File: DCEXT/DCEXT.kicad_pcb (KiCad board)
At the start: 2 copper layers, 77 x 100.5 mm, 5 parts, among them U1 MPCIE-Socket

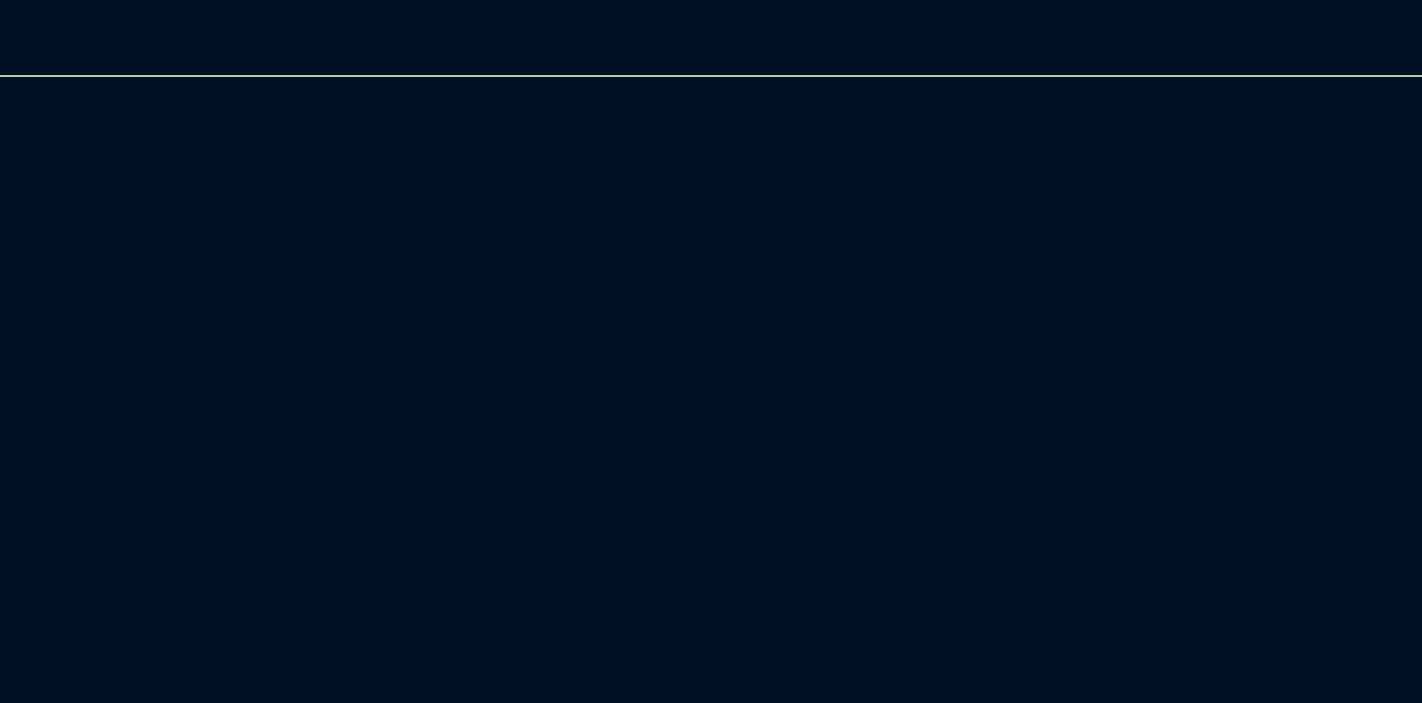
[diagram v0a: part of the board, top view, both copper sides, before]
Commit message: Add usb host connector and add more documentation
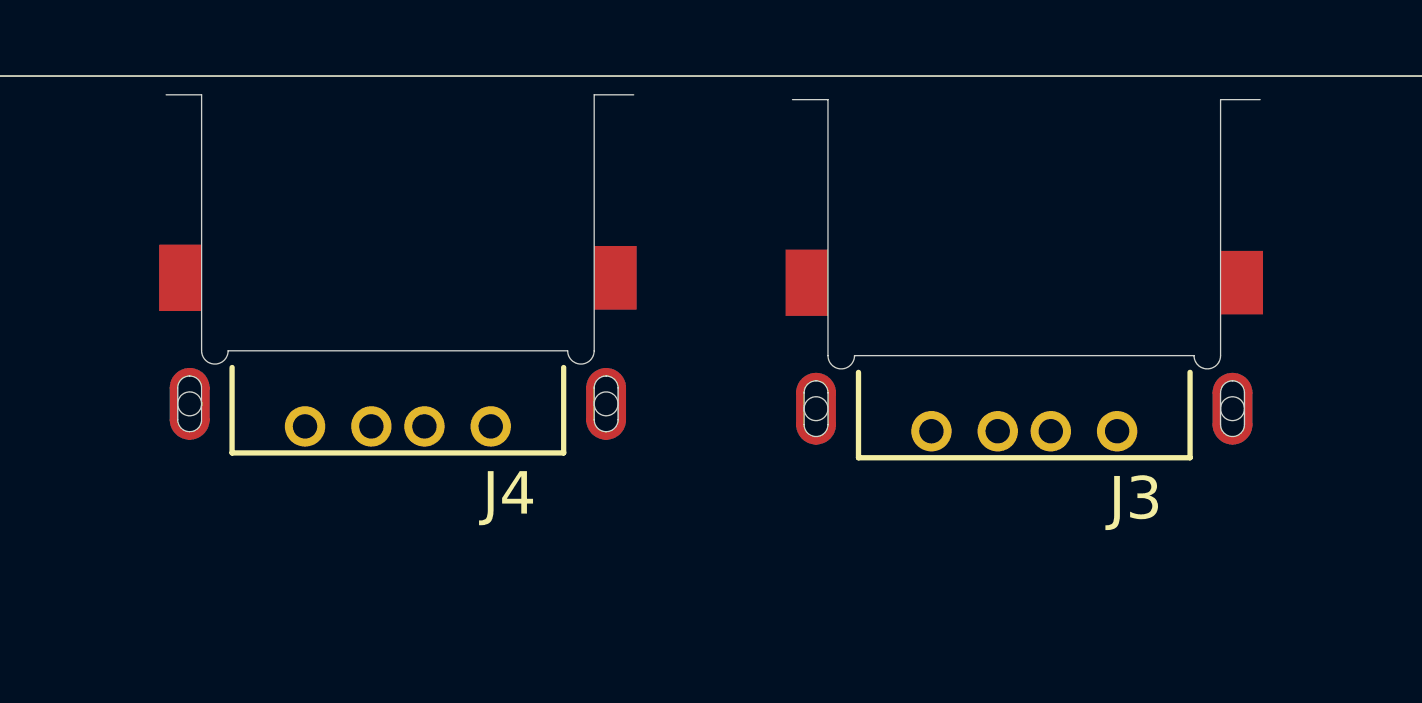
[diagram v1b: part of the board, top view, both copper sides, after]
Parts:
- added J3: USB1015-XX-X-X_REVC, DCEXT:GCT_USB1015-XX-X-X_REVC, F.Cu at (110.0, 49.5)
- added J4: USB1015-XX-X-X_REVC, DCEXT:GCT_USB1015-XX-X-X_REVC, F.Cu at (86.4, 49.3)
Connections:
- H1 pad 1: Net-(H1-Pad1) -> GND
- H2 pad 1: Net-(H2-Pad1) -> GND
- H3 pad 1: Net-(H3-Pad1) -> GND
- H4 pad 1: Net-(H4-Pad1) -> GND

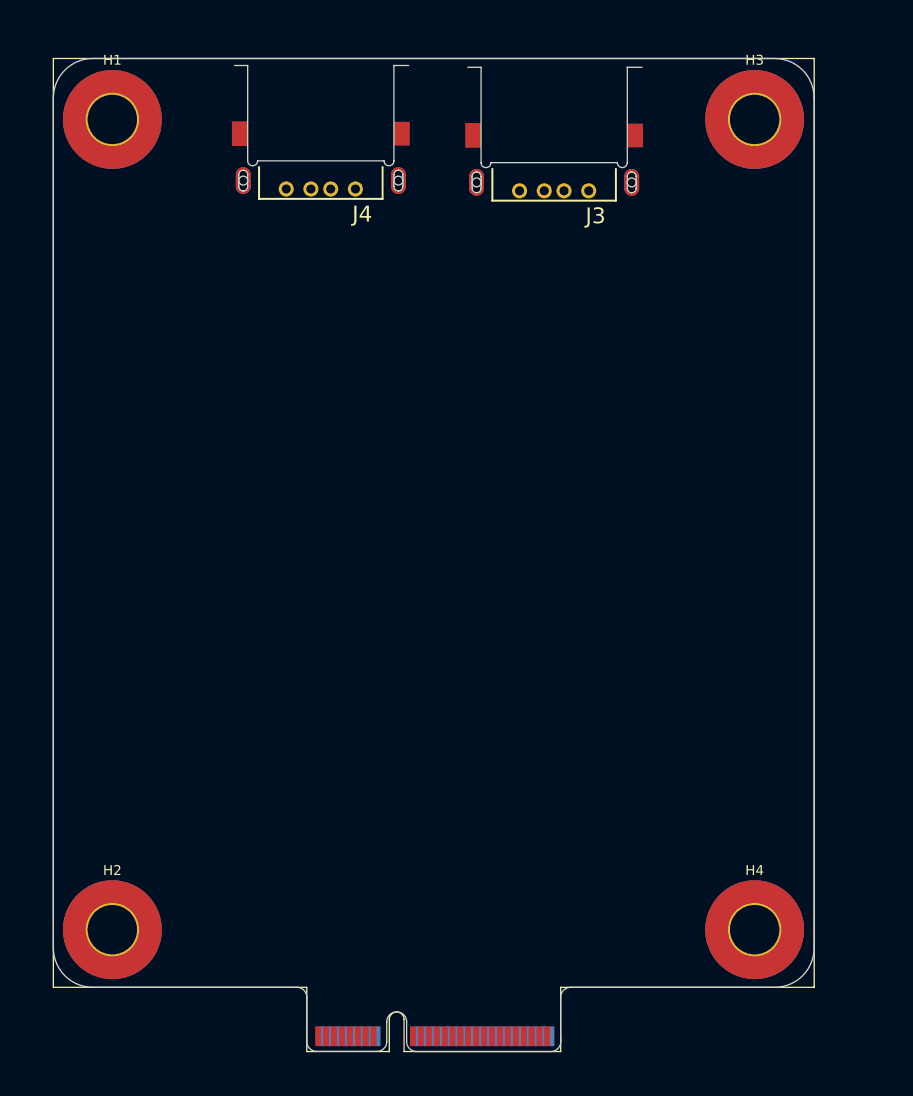
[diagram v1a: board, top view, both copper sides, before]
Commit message: Add usb protection, fan control and fpc connector for module
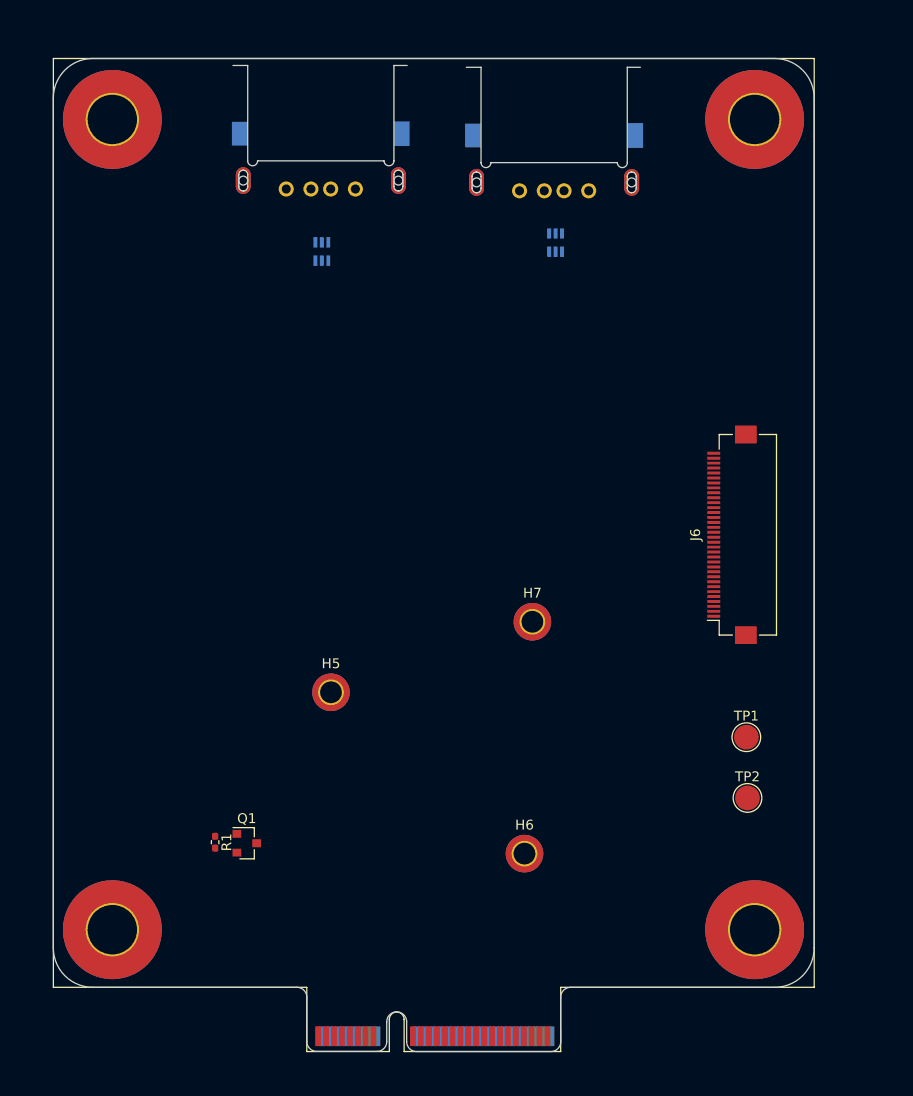
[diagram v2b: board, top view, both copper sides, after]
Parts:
- added H5: MountingHole_Pad, MountingHole:MountingHole_2.2mm_M2_DIN965_Pad_TopBottom, F.Cu at (87.4, 106.3)
- added H6: MountingHole_Pad, MountingHole:MountingHole_2.2mm_M2_DIN965_Pad_TopBottom, F.Cu at (107.0, 122.6)
- added H7: MountingHole_Pad, MountingHole:MountingHole_2.2mm_M2_DIN965_Pad_TopBottom, F.Cu at (107.8, 99.1)
- added J6: Conn_02x17_Odd_Even, Connector_FFC-FPC:Hirose_FH12-34S-0.5SH_1x34-1MP_P0.50mm_Horizontal, F.Cu at (128.0, 90.3)
- added Q1: SI2310, Package_TO_SOT_SMD:SOT-23, F.Cu at (78.9, 121.6)
- added R1: R, Resistor_SMD:R_0402_1005Metric_Pad0.72x0.64mm_HandSolder, F.Cu at (75.7, 121.5)
- added TP1: UART_RX, TestPoint:TestPoint_Pad_D2.5mm, F.Cu at (129.4, 110.8)
- added TP2: UART_TX, TestPoint:TestPoint_Pad_D2.5mm, F.Cu at (129.5, 117.0)
- added U2: USBUF02W6, eec:ST_Microelectronics-USBUF02W6-0, B.Cu at (110.1, 60.8)
- added U3: USBUF02W6, eec:ST_Microelectronics-USBUF02W6-0, B.Cu at (86.5, 61.7)
- J3, J4: moved to B.Cu
- turned J3 to 0 degrees
- turned J4 to 0 degrees
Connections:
- net Net-(U1-Pad1) renamed /SPK_LP
- net Net-(U1-Pad3) renamed /SPK_LN
- J3 pad 1: Net-(J3-Pad1) -> /USB_5V
- J3 pad 4: Net-(J3-Pad4) -> GND
- J3 pad 5: Net-(J3-Pad5) -> GND
- J3 pad 6: Net-(J3-Pad5) -> GND
- J3 pad 7: Net-(J3-Pad5) -> GND
- J3 pad 8: Net-(J3-Pad5) -> GND
- J4 pad 1: Net-(J4-Pad1) -> /USB_5V
- J4 pad 4: Net-(J4-Pad4) -> GND
- J4 pad 5: Net-(J4-Pad5) -> GND
- J4 pad 6: Net-(J4-Pad5) -> GND
- J4 pad 7: Net-(J4-Pad5) -> GND
- J4 pad 8: Net-(J4-Pad5) -> GND
- U1 pad 11: Net-(U1-Pad11) -> GND
- U1 pad 13: Net-(U1-Pad13) -> /USB4_D_N
- U1 pad 15: Net-(U1-Pad15) -> /USB4_D_P
- U1 pad 17: Net-(U1-Pad17) -> +3V3
- U1 pad 19: Net-(U1-Pad19) -> +3V3
- U1 pad 5: Net-(U1-Pad5) -> GND
- U1 pad 7: Net-(U1-Pad7) -> /USB3_D_N
- U1 pad 9: Net-(U1-Pad9) -> /USB3_D_P

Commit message: Fix usb position,holes and pcb outline, add current limiter
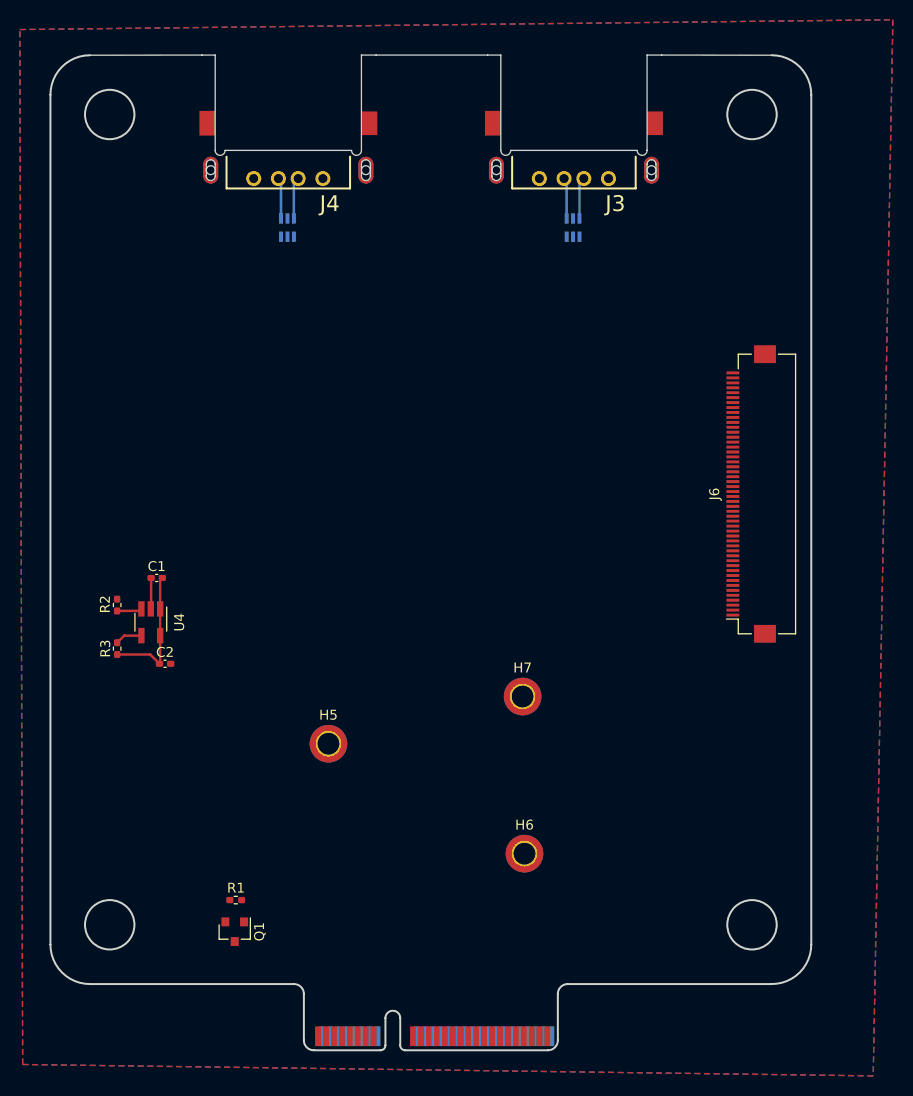
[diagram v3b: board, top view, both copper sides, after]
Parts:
- removed H1, H2, H3, H4: MountingHole_Pad, MountingHole:MountingHole_5mm_Pad_TopBottom
- removed TP1: UART_RX, TestPoint:TestPoint_Pad_D2.5mm
- removed TP2: UART_TX, TestPoint:TestPoint_Pad_D2.5mm
- added C1: 10uF, Capacitor_SMD:C_0402_1005Metric_Pad0.74x0.62mm_HandSolder, F.Cu at (69.7, 94.7)
- added C2: 10uF, Capacitor_SMD:C_0402_1005Metric_Pad0.74x0.62mm_HandSolder, F.Cu at (70.6, 103.4)
- added R2: 6.8K 1%, Resistor_SMD:R_0402_1005Metric_Pad0.72x0.64mm_HandSolder, F.Cu at (65.7, 97.4)
- added R3: 10K, Resistor_SMD:R_0402_1005Metric_Pad0.72x0.64mm_HandSolder, F.Cu at (65.7, 101.9)
- added U4: SY6280, Package_TO_SOT_SMD:SOT-23-5_HandSoldering, F.Cu at (69.2, 99.2)
- J3, J4: moved to F.Cu
- J6: value Conn_02x17_Odd_Even -> Conn_02x25_Odd_Even; footprint Connector_FFC-FPC:Hirose_FH12-34S-0.5SH_1x34-1MP_P0.50mm_Horizontal -> Connector_FFC-FPC:Hirose_FH12-50S-0.5SH_1x50-1MP_P0.50mm_Horizontal
- R1: value R -> 10K
- U1: value MPCIE-Socket -> MPCIE-DevTerm
- moved Q1 9.04 mm to (77.6, 130.5), turned to 270 degrees
- moved H7 7.63 mm to (106.8, 106.7)
- moved R1 6.21 mm to (77.7, 127.3), turned to 180 degrees
- moved H5 5.21 mm to (87.1, 111.5)
- moved J6 4.56 mm to (129.9, 86.2)
- moved U3 4.24 mm to (83.0, 59.2), turned to 90 degrees
- moved J4 3.45 mm to (83.1, 48.3), turned to 180 degrees
- moved J3 2.35 mm to (112.0, 48.3), turned to 180 degrees
- moved U2 2.33 mm to (111.9, 59.2), turned to 90 degrees
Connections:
- net Net-(U1-Pad14) renamed /SPK_RP
- net Net-(U1-Pad16) renamed /SPK_RN
- J6 pad 1: Net-(J6-Pad1) -> /GPIO34
- J6 pad 10: Net-(J6-Pad10) -> /GPIO41
- J6 pad 11: Net-(J6-Pad11) -> /GPIO29
- J6 pad 12: Net-(J6-Pad12) -> /GPIO40
- J6 pad 13: Net-(J6-Pad13) -> /GPIO28
- J6 pad 14: Net-(J6-Pad14) -> /GPIO39
- J6 pad 15: Net-(J6-Pad15) -> +3V3
- J6 pad 16: Net-(J6-Pad16) -> /GPIO38
- J6 pad 17: Net-(J6-Pad17) -> +5V
- J6 pad 18: Net-(J6-Pad18) -> /GPIO37
- J6 pad 19: Net-(J6-Pad19) -> GND
- J6 pad 2: Net-(J6-Pad2) -> /GPIO45
- J6 pad 20: Net-(J6-Pad20) -> /GPIO36
- J6 pad 21: Net-(J6-Pad21) -> /CAM1_D0_N
- J6 pad 22: Net-(J6-Pad22) -> /GPIO35
- J6 pad 23: Net-(J6-Pad23) -> /CAM1_D0_P
- J6 pad 24: Net-(J6-Pad24) -> +3V3
- J6 pad 25: Net-(J6-Pad25) -> GND
- J6 pad 26: Net-(J6-Pad26) -> +5V
- J6 pad 27: Net-(J6-Pad27) -> /CAM1_D1_N
- J6 pad 28: Net-(J6-Pad28) -> /UART_RX
- J6 pad 29: Net-(J6-Pad29) -> /CAM1_D1_P
- J6 pad 3: Net-(J6-Pad3) -> /GPIO33
- J6 pad 30: Net-(J6-Pad30) -> /UART_TX
- J6 pad 31: Net-(J6-Pad31) -> GND
- J6 pad 33: Net-(J6-Pad33) -> /CAM1_C_N
- J6 pad 4: Net-(J6-Pad4) -> /GPIO44
- J6 pad 5: Net-(J6-Pad5) -> /GPIO32
- J6 pad 6: Net-(J6-Pad6) -> /GPIO43
- J6 pad 7: Net-(J6-Pad7) -> /GPIO31
- J6 pad 8: Net-(J6-Pad8) -> /GPIO42
- J6 pad 9: Net-(J6-Pad9) -> /GPIO30
- U1 pad 10: Net-(U1-Pad10) -> +5V
- U1 pad 12: Net-(U1-Pad12) -> GND
- U1 pad 18: Net-(U1-Pad18) -> /GPIO28
- U1 pad 2: Net-(U1-Pad2) -> +5V
- U1 pad 20: Net-(U1-Pad20) -> /GPIO29
- U1 pad 21: Net-(U1-Pad21) -> GND
- U1 pad 22: Net-(U1-Pad22) -> /GPIO30
- U1 pad 23: Net-(U1-Pad23) -> /CAM1_D3_P
- U1 pad 24: Net-(U1-Pad24) -> /GPIO31
- U1 pad 25: Net-(U1-Pad25) -> /CAM1_D3_N
- U1 pad 26: Net-(U1-Pad26) -> /GPIO32
- U1 pad 27: Net-(U1-Pad27) -> GND
- U1 pad 28: Net-(U1-Pad28) -> /GPIO33
- U1 pad 29: Net-(U1-Pad29) -> /CAM1_D2_P
- U1 pad 30: Net-(U1-Pad30) -> /GPIO34
- U1 pad 31: Net-(U1-Pad31) -> /CAM1_D2_N
- U1 pad 32: Net-(U1-Pad32) -> /GPIO35
- U1 pad 33: Net-(U1-Pad33) -> GND
- U1 pad 34: Net-(U1-Pad34) -> /GPIO36
- U1 pad 35: Net-(U1-Pad35) -> /CAM1_C_P
- U1 pad 36: Net-(U1-Pad36) -> /GPIO37
- U1 pad 37: Net-(U1-Pad37) -> /CAM1_C_N
- U1 pad 38: Net-(U1-Pad38) -> /GPIO38
- U1 pad 39: Net-(U1-Pad39) -> GND
- U1 pad 4: Net-(U1-Pad4) -> +5V
- U1 pad 40: Net-(U1-Pad40) -> /GPIO39
- U1 pad 41: Net-(U1-Pad41) -> /CAM1_D1_P
- U1 pad 42: Net-(U1-Pad42) -> /GPIO40
- U1 pad 43: Net-(U1-Pad43) -> /CAM1_D1_N
- U1 pad 44: Net-(U1-Pad44) -> /GPIO41
- U1 pad 45: Net-(U1-Pad45) -> GND
- U1 pad 46: Net-(U1-Pad46) -> /GPIO42
- U1 pad 47: Net-(U1-Pad47) -> /CAM1_D0_P
- U1 pad 48: Net-(U1-Pad48) -> /GPIO43
- U1 pad 49: Net-(U1-Pad49) -> /CAM1_D0_N
- U1 pad 50: Net-(U1-Pad50) -> /GPIO44
- U1 pad 51: Net-(U1-Pad51) -> GND
- U1 pad 52: Net-(U1-Pad52) -> /GPIO45
- U1 pad 6: Net-(U1-Pad6) -> +5V
- U1 pad 8: Net-(U1-Pad8) -> +5V
- U2 pad 1: /USB3_D_N -> /USB4_D_N
- U2 pad 3: /USB3_D_P -> /USB4_D_P
- U3 pad 1: /USB4_D_N -> /USB3_D_N
- U3 pad 3: /USB4_D_P -> /USB3_D_P
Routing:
- net +5V: track 0.00 -> 13.5 mm
- net Net-(J4-Pad2): track 0.00 -> 4.22 mm
- net Net-(J3-Pad2): track 0.00 -> 4.22 mm
- net Net-(J4-Pad3): track 0.00 -> 4.14 mm
- net Net-(J3-Pad3): track 0.00 -> 4.14 mm
- net GND: track 0.00 -> 3.15 mm
- net Net-(R3-Pad2): track 0.00 -> 2.75 mm
- net Net-(R2-Pad2): track 0.00 -> 2.54 mm
- added copper zone on B.Cu, net GND
- added copper zone on F.Cu, net GND
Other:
- board size 77 x 100.5 mm -> 77 x 100.7 mm
- board text added: "1.00"
- board text added: "25.65"
- board text added: "25.70"
- board text added: "4-5.00"
- board text added: "4.00"
- board text added: "5.00"
- board text added: "52.00"
- board text added: "61.00"
- board text added: "65.00"
- board text added: "77.00"
- board text added: "82.00"
- board text added: "94.00"

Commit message: Progess
Pop OS and kicad decided i didnt need 3d acceleration anymore, switching to mac
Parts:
- removed H5, H6, H7: MountingHole_Pad, MountingHole:MountingHole_2.2mm_M2_DIN965_Pad_TopBottom
- Q1, R1: moved to B.Cu
- moved R1 4.47 mm to (74.0, 124.9), turned to 0 degrees
- moved Q1 4.31 mm to (74.1, 128.1)
- moved U3 1.14 mm to (84.1, 59.2)
- moved J3 1.10 mm to (110.9, 48.3)
- moved J4 1.04 mm to (84.1, 48.3)
- moved U2 0.99 mm to (110.9, 59.2)
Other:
- outline, holes or cut-outs redrawn
